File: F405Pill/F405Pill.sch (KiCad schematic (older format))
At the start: 112 parts, among them IC1 VREG-3V3, SW1 !RST, SW2 BOOT, U1 STM32F405RGT, Y1 8MHz

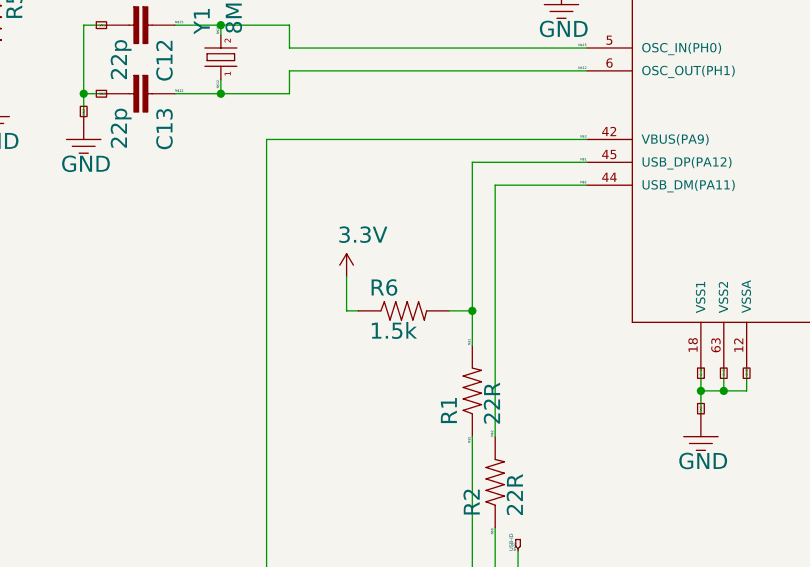
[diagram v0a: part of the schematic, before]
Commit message: removed unnecessary USB pullup resistor from STM32F4STAMP
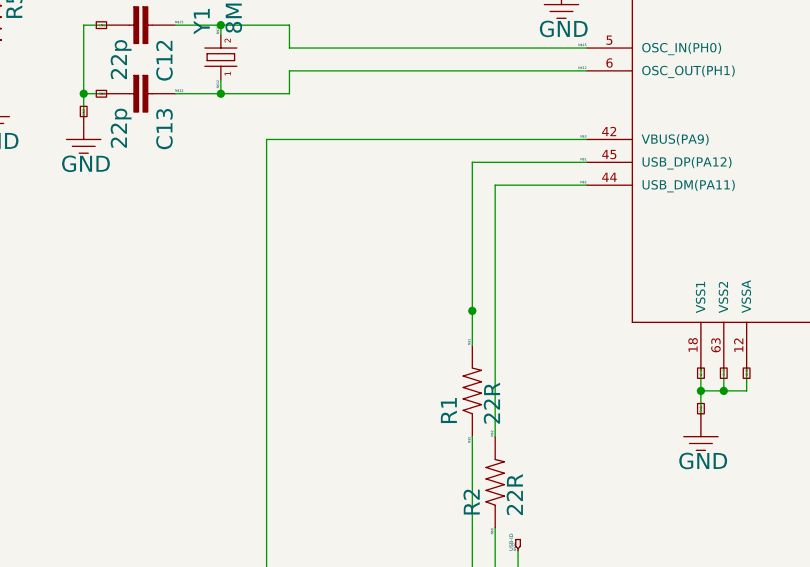
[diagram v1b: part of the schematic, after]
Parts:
- removed R6: 1.5k, F405Pill:0603-RES, symbol RESISTOR0603-RES
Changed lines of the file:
@@
 Text Label 21800 15600 1    10   ~ 0
 N$63
-$Comp
-L RESISTOR0603-RES R6
-U 1 1 59CDCB31
-P 20500 18650
-F 0 "R6" H 20350 18709 70  0000 L BNN
-F 1 "1.5k" H 20350 18520 70  0000 L BNN
-F 2 "F405Pill:0603-RES" H 20490 18440 65  0001 L TNN
-F 3 "" H 20500 18650 60  0001 C CNN
-	1    20500 18650
-	1    0    0    -1
-$EndComp
-Wire Wire Line
-	20800 18650 20700 18650
 Connection ~ 20800 18650
-$Comp
-L 3.3V #P+021
-U 1 1 59CDD7F4
-P 20250 18500
-F 0 "#P+021" H 20211 18640 70  0001 L BNN
-F 1 "3.3V" H 20211 18640 70  0000 L BNN
-F 2 "" H 20250 18500 60  0001 C CNN
-F 3 "" H 20250 18500 60  0001 C CNN
-	1    20250 18500
-	1    0    0    -1
-$EndComp
-Wire Wire Line
-	20300 18650 20250 18650
-Wire Wire Line
-	20250 18650 20250 18500
 $EndSCHEMATC
